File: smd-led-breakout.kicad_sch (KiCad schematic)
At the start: 13 parts

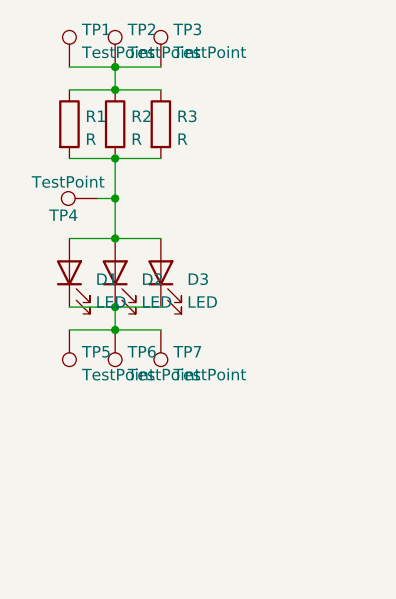
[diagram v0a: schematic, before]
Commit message: Added bridge for measuring current.
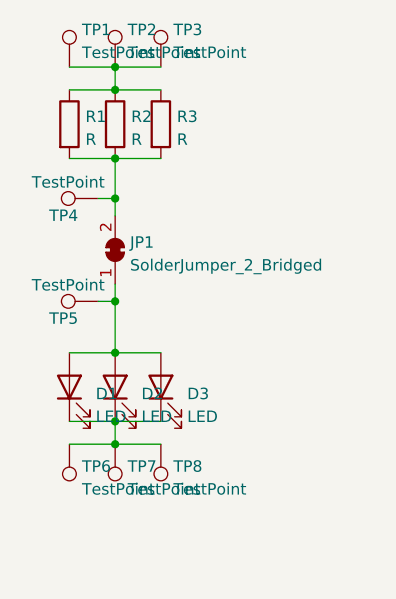
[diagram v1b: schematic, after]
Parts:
- added JP1: SolderJumper_2_Bridged, _:SolderJumper-2_P1.3mm_Bridged_Pad1.0x1.5mm, symbol Jumper:SolderJumper_2_Bridged
- added TP5: TestPoint, Connector_Pin:Pin_D1.0mm_L10.0mm, symbol Connector:TestPoint
- renumbered TP5 to TP6, TP6 to TP7, TP7 to TP8
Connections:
- net at R1.2, R2.2, R3.2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: now also JP1.2 (B); no longer D1.2 (A), D2.2 (A), D3.2 (A)
- new net: D1.2 (A), D2.2 (A), D3.2 (A), JP1.1 (A), TP5.1
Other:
- moved on the sheet: D1, D2, D3, TP6, TP7, TP8

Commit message: Refinements
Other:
- moved on the sheet: TP6, TP7, TP8
